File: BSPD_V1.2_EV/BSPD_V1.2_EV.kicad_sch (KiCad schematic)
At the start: 62 parts, among them IC1 LM2901BIRTER, IC2 LM2901BIRTER, IC3 74AHC1G08, IC4 SN74HC32PWR, IC5 L7805ACD2T-TR, J1 776280-1, Q1 2N7002,215

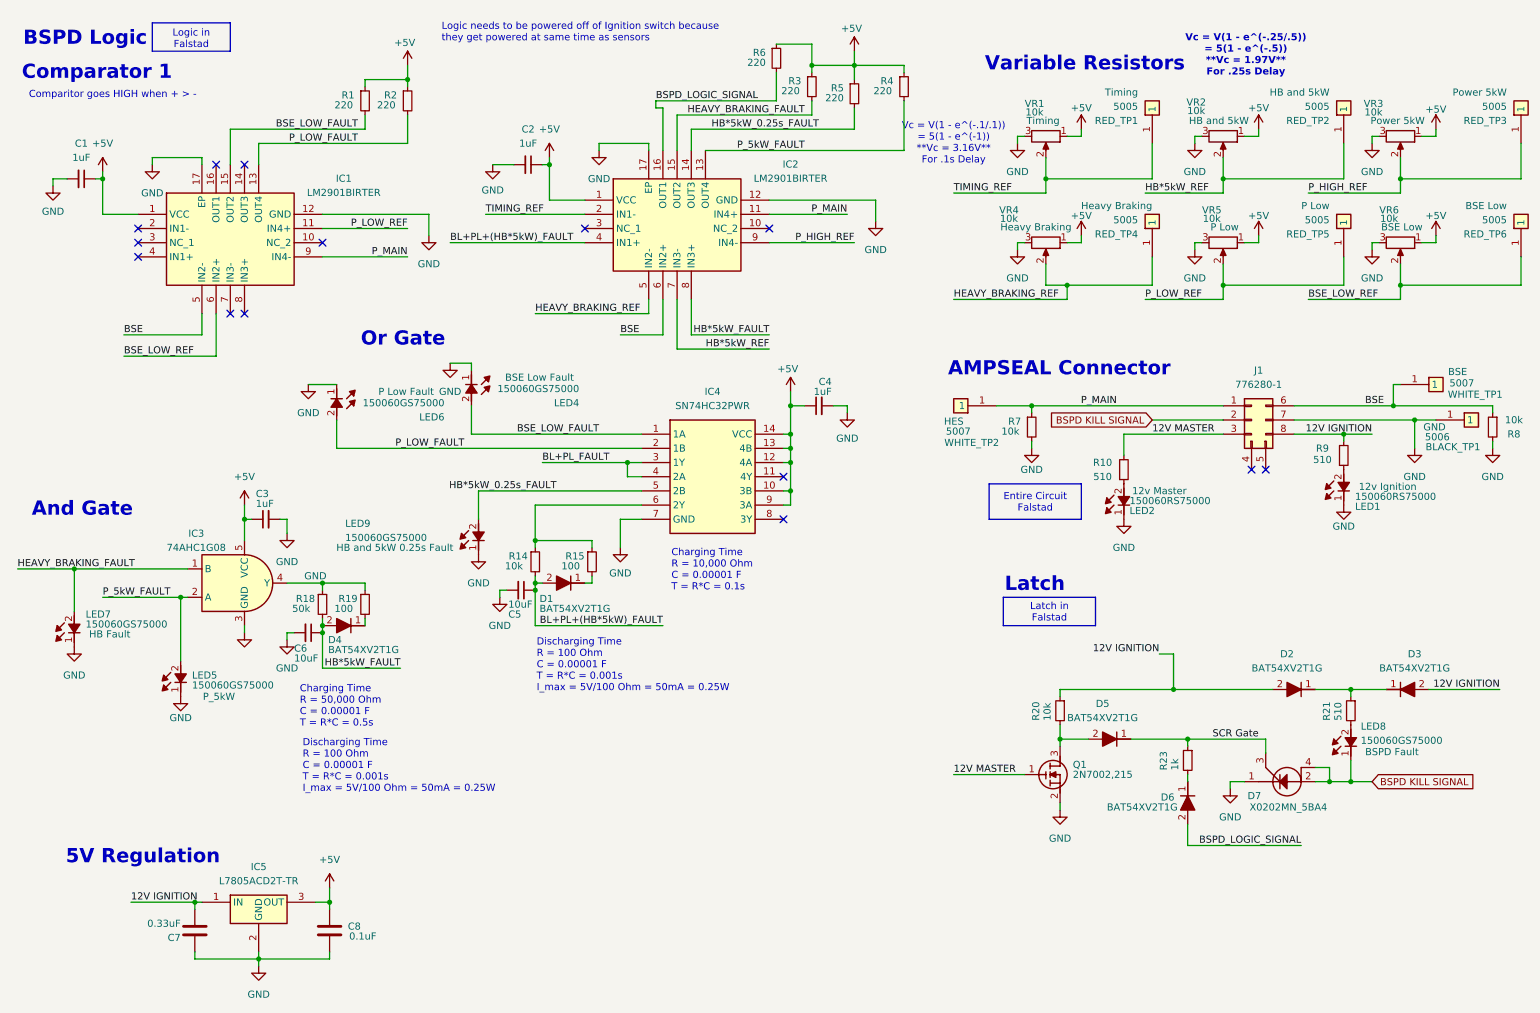
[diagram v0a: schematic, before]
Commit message: BSPD, Shutdown/Charging Shutdown, & Voltage Indicator final changes
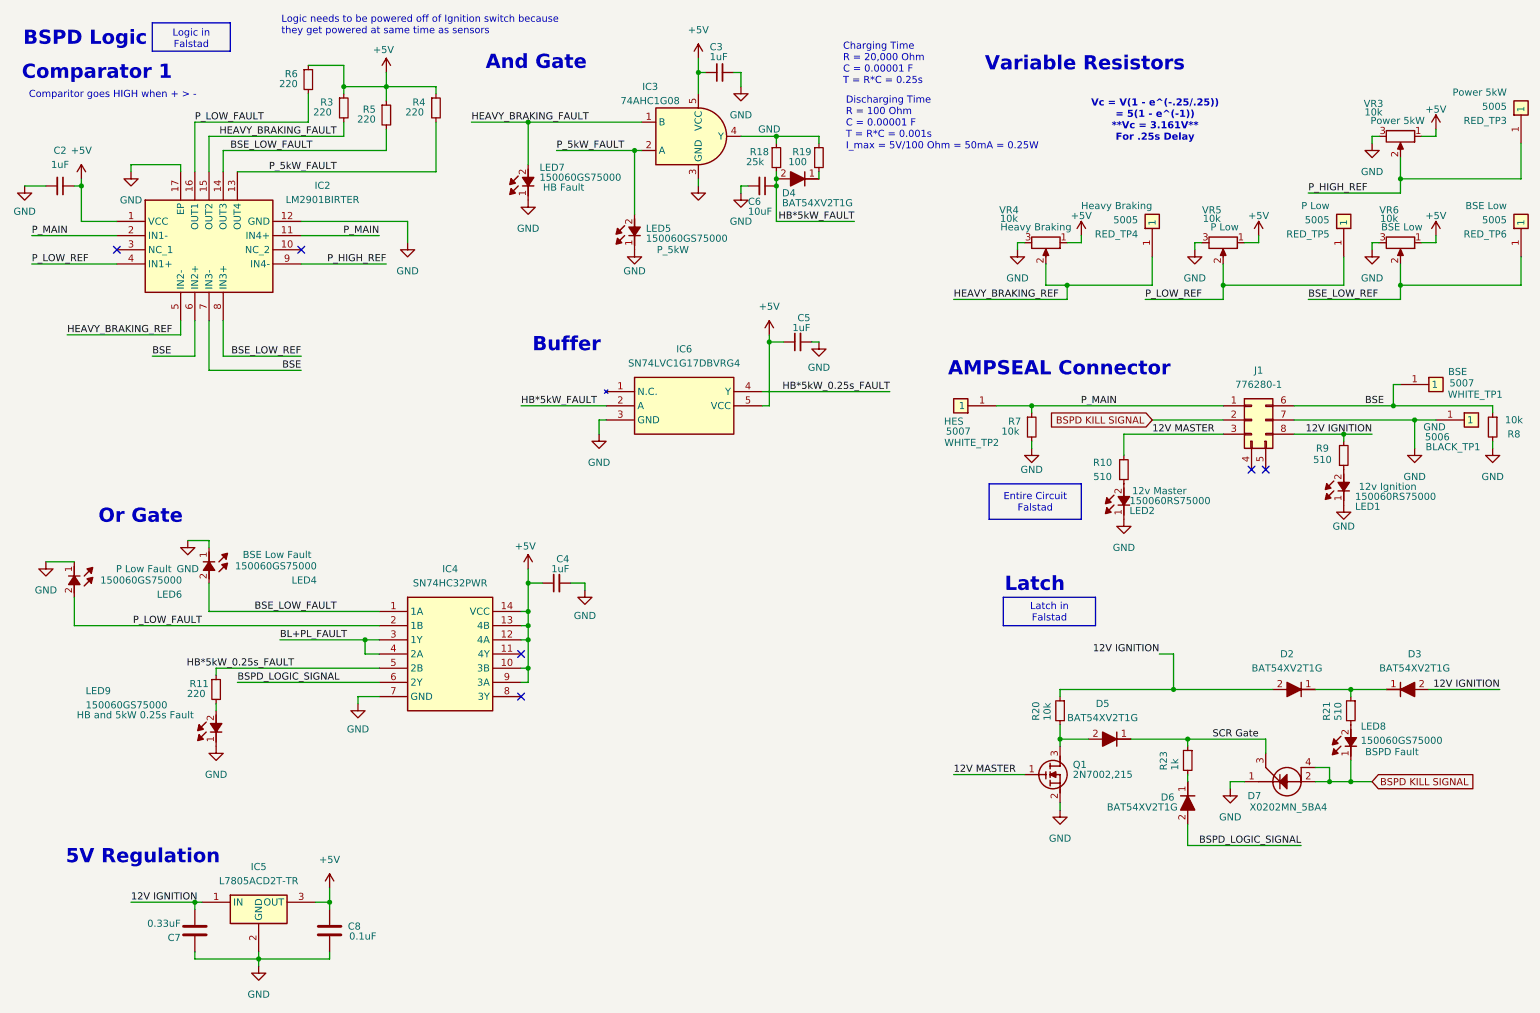
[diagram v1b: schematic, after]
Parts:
- removed C1: 1uF, Capacitor_SMD:C_0603_1608Metric, symbol Device:C_Small
- removed D1: BAT54XV2T1G, SDM_MiscFootprint:SODFL1608X70N, symbol SDM_DIODES:BAT54XV2T1G
- removed IC1: LM2901BIRTER, SDM_MiscFootprint:QFN50P300X300X80-17N-D, symbol SDM_COMPARITOR:LM2901BIRTER
- removed R1, R2: 220, Resistor_SMD:R_0603_1608Metric, symbol Device:R_Small
- removed R14: 10k, Resistor_SMD:R_0603_1608Metric, symbol Device:R_Small
- removed R15: 100, Resistor_SMD:R_0603_1608Metric, symbol Device:R_Small
- removed RED_TP1, RED_TP2: 5005, SDM_MiscFootprint:5005, symbol SDM_TESTPOINT:5005
- removed VR1, VR2: 10k, SDM_MiscFootprint:3386P1103TLF, symbol SDM_VARIABLE_RESISTOR:3386P-1-103TLF
- added IC6: SN74LVC1G17DBVRG4, Misc:SOT95P280X145-5N, symbol Misc:SN74LVC1G17DBVRG4
- added R11: 220, Resistor_SMD:R_0603_1608Metric, symbol Device:R_Small
- C5: value 10uF -> 1uF
- R18: value 50k -> 25k
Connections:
- net HB*5kW_REF is gone; now on net BSE: IC2.7 (IN3-)
- net TIMING_REF is gone; now on net P_MAIN: IC2.2 (IN1-)
- net +5V: now also C5.1, IC6.5 (VCC)
- net BSE_LOW_FAULT: now also IC2.14 (OUT3), R5.2
- net BSE_LOW_REF: now also IC2.8 (IN3+)
- net BSPD_LOGIC_SIGNAL: now also IC4.6 (2Y); no longer IC2.16 (OUT1), R6.2
- net GND: now also IC6.3 (GND)
- net HB*5kW_0.25s_FAULT: now also IC6.4 (Y), R11.1; no longer IC2.14 (OUT3), LED9.2 (A), R5.2
- net HB*5kW_FAULT: now also IC6.2 (A); no longer IC2.8 (IN3+)
- net P_LOW_FAULT: now also IC2.16 (OUT1), R6.2
- net P_LOW_REF: now also IC2.4 (IN1+)
- removed net BL+PL+(HB*5kW)_FAULT: C5.1, IC2.4 (IN1+)
- new net: LED9.2 (A), R11.2
- no-connect marks 14 -> 6
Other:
- note added: "Buffer"
- note added: "Charging Time R = 20,000 Ohm C = 0.00001 F T = R*C = 0.25s"
- note added: "Vc = V(1 - e^(-.25/.25)) = 5(1 - e^(-1)) **Vc = 3.161V** For .25s Delay"
- note removed: "Charging Time R = 10,000 Ohm C = 0.00001 F T = R*C = 0.1s"
- note removed: "Charging Time R = 50,000 Ohm C = 0.00001 F T = R*C = 0.5s"
- note removed: "Vc = V(1 - e^(-.1/.1)) = 5(1 - e^(-1)) **Vc = 3.16V** For .1s Delay"
- note removed: "Vc = V(1 - e^(-.25/.5)) = 5(1 - e^(-.5)) **Vc = 1.97V** For .25s Delay"
- moved on the sheet: C2, C3, C4, C6, D4, IC2, IC3, IC4, LED4, LED5, LED6, LED7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

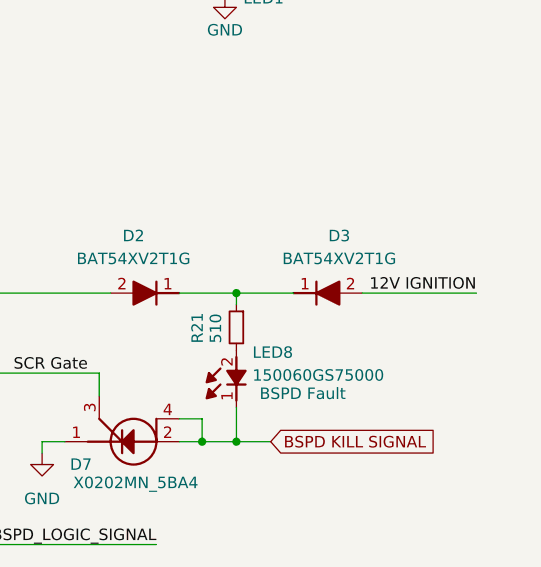
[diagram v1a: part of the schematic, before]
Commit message: Fixed a net in BSPD and added isolated 5V line in voltage indicator
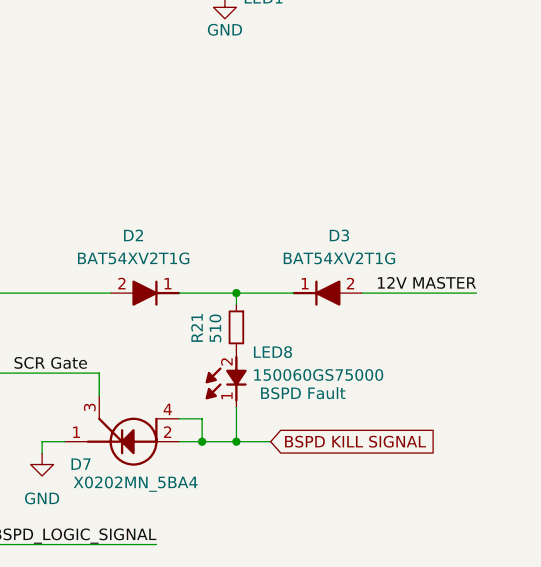
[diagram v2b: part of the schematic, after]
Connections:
- net 12V IGNITION: no longer D3.2 (A)
- net 12V MASTER: now also D3.2 (A)
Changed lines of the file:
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@@
 		)
 	)
-	(label "12V IGNITION"
+	(label "12V MASTER"
 		(at 279.4 134.62 180)
 		(effects
